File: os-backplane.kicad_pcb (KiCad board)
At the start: 4 copper layers, 195 x 95 mm, 161 parts, among them J1 FPANEL, J2 FAN, J3 PWR, Q1 IRFML8244, Q10 CSD18503Q5A, Q11 MMUN2231L, Q2 AOD4189, Q3 AOD4189, Q4 MMBT3906, Q5 MMBT3904, Q6 MMBT3904, Q7 CSD18504Q5A, Q8 MMUN2231L, Q9 CSD18504Q5A, U1 LM25116MHX, U2 LM25088-1MH

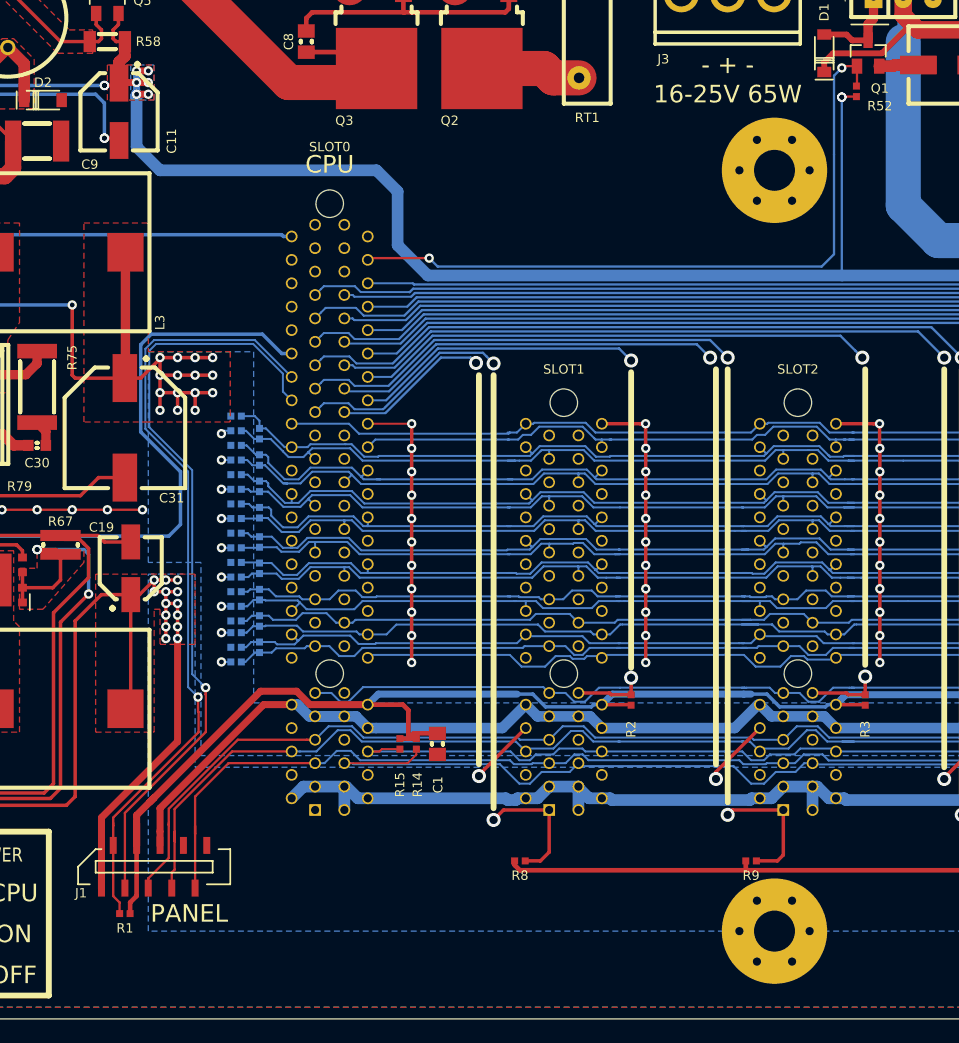
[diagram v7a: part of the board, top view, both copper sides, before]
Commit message: Added power supply load test points
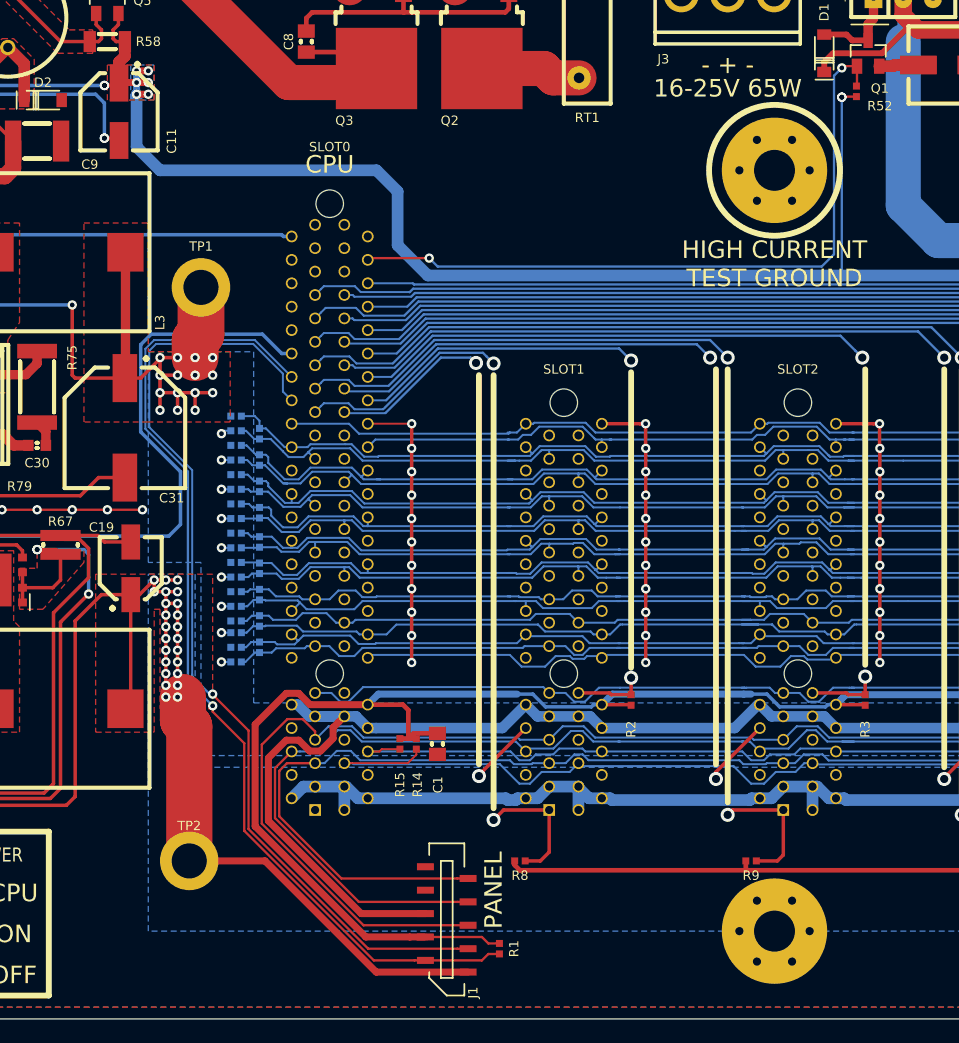
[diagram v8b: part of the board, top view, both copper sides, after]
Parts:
- added TP1: 3V3, conn-test:TEST-PTH, F.Cu at (76.0, 90.0)
- added TP2: 12V, conn-test:TEST-PTH, F.Cu at (75.0, 139.0)
- moved R1 32.1 mm to (101.5, 146.5), turned to 90 degrees
- moved J1 25.4 mm to (97.0, 144.0), turned to 90 degrees
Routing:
- net +12: track 423.2 -> 452.2 mm, vias 14 -> 24
- net +3.3: track 231.9 -> 251.4 mm
- net /#IRQ_FP: track 67.8 -> 85.4 mm
- net /SPI_#CS_FP: track 66.1 -> 82.8 mm
- net /SPI_MISO: track 148.8 -> 160.7 mm
- net +3.3SB: track 554.1 -> 563.2 mm
- net /SPI_MOSI: track 152.2 -> 158.3 mm
- net /SPI_CLK: track 144.4 -> 150.0 mm
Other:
- board text added: "HIGH CURRENT TEST GROUND"
